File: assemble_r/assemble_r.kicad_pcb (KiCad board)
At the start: 2 copper layers, 57 parts, among them J1 Conn_01x02_Pin, SW29 SW_Push, SW30 SW_Push, SW31 SW_Push, SW32 SW_Push, SW33 SW_Push, SW34 SW_Push, SW35 SW_Push, SW36 SW_Push, SW37 SW_Push, SW38 SW_Push, SW39 SW_Push, SW40 SW_Push, SW41 SW_Push, SW42 SW_Push, SW43 SW_Push, SW44 SW_Push, SW45 SW_Push, SW46 SW_Push, SW47 SW_Push, SW48 SW_Push, SW49 SW_Push, SW50 SW_Push, SW51 SW_Push, SW52 SW_Push, SW53 SW_Push, SW54 SW_Push, SW55 SW_Push, SW56 SW_Push, U1 Micon_BLEMicroPro

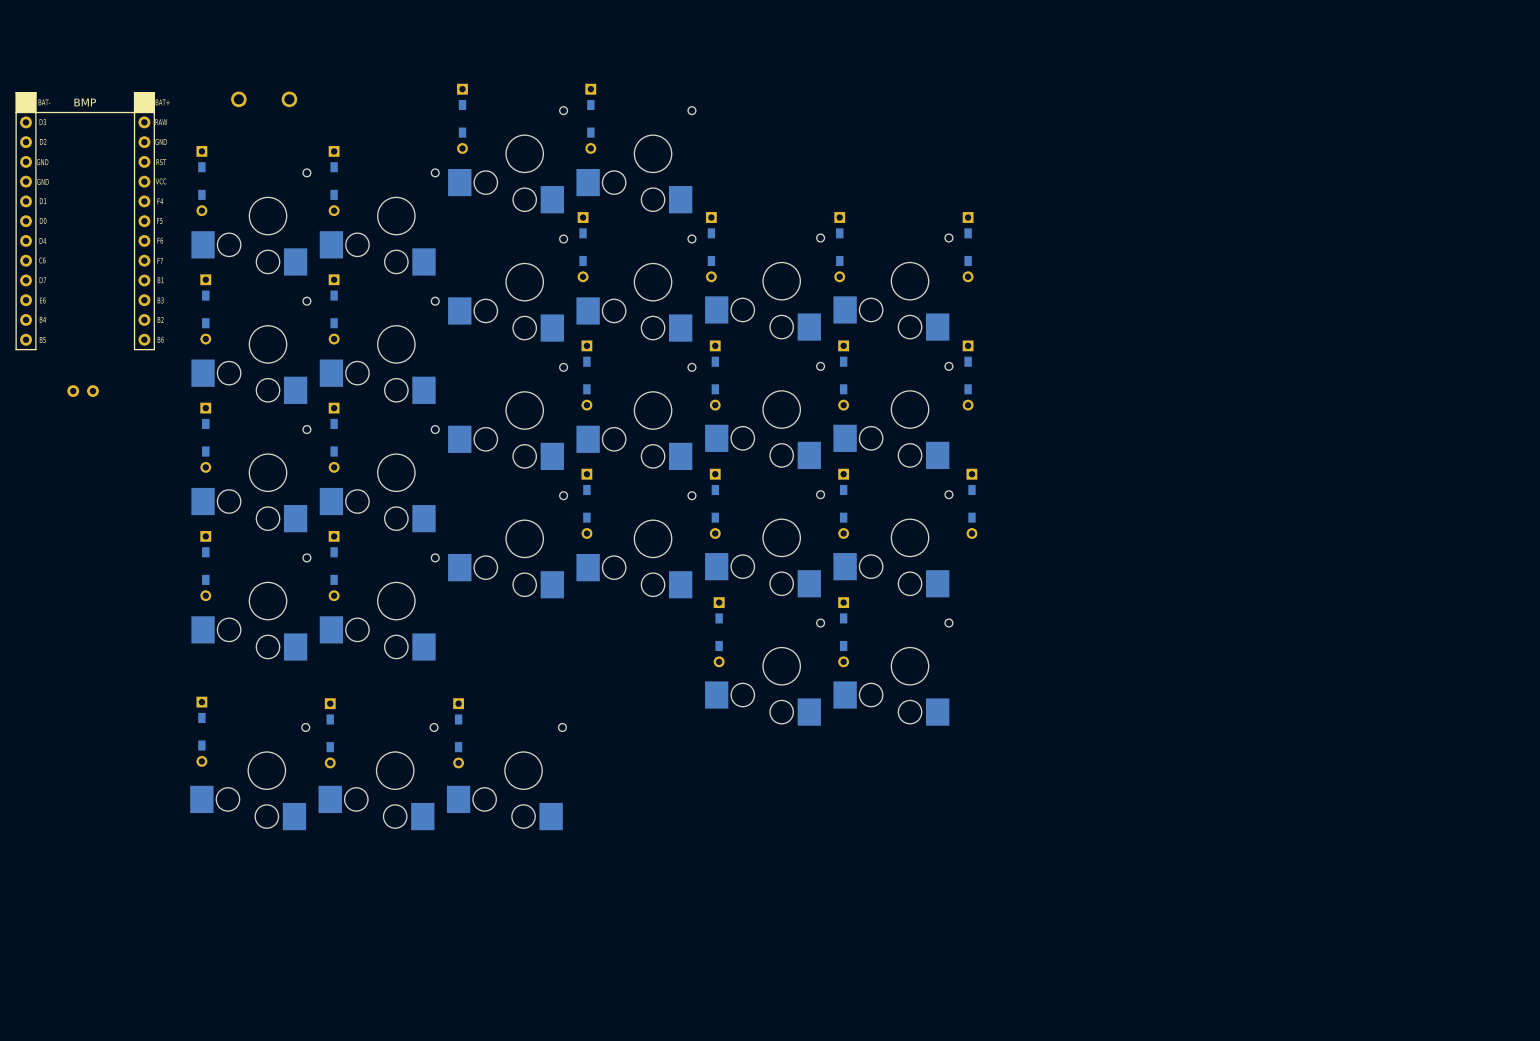
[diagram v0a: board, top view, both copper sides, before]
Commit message: feat: add PCB for right hand
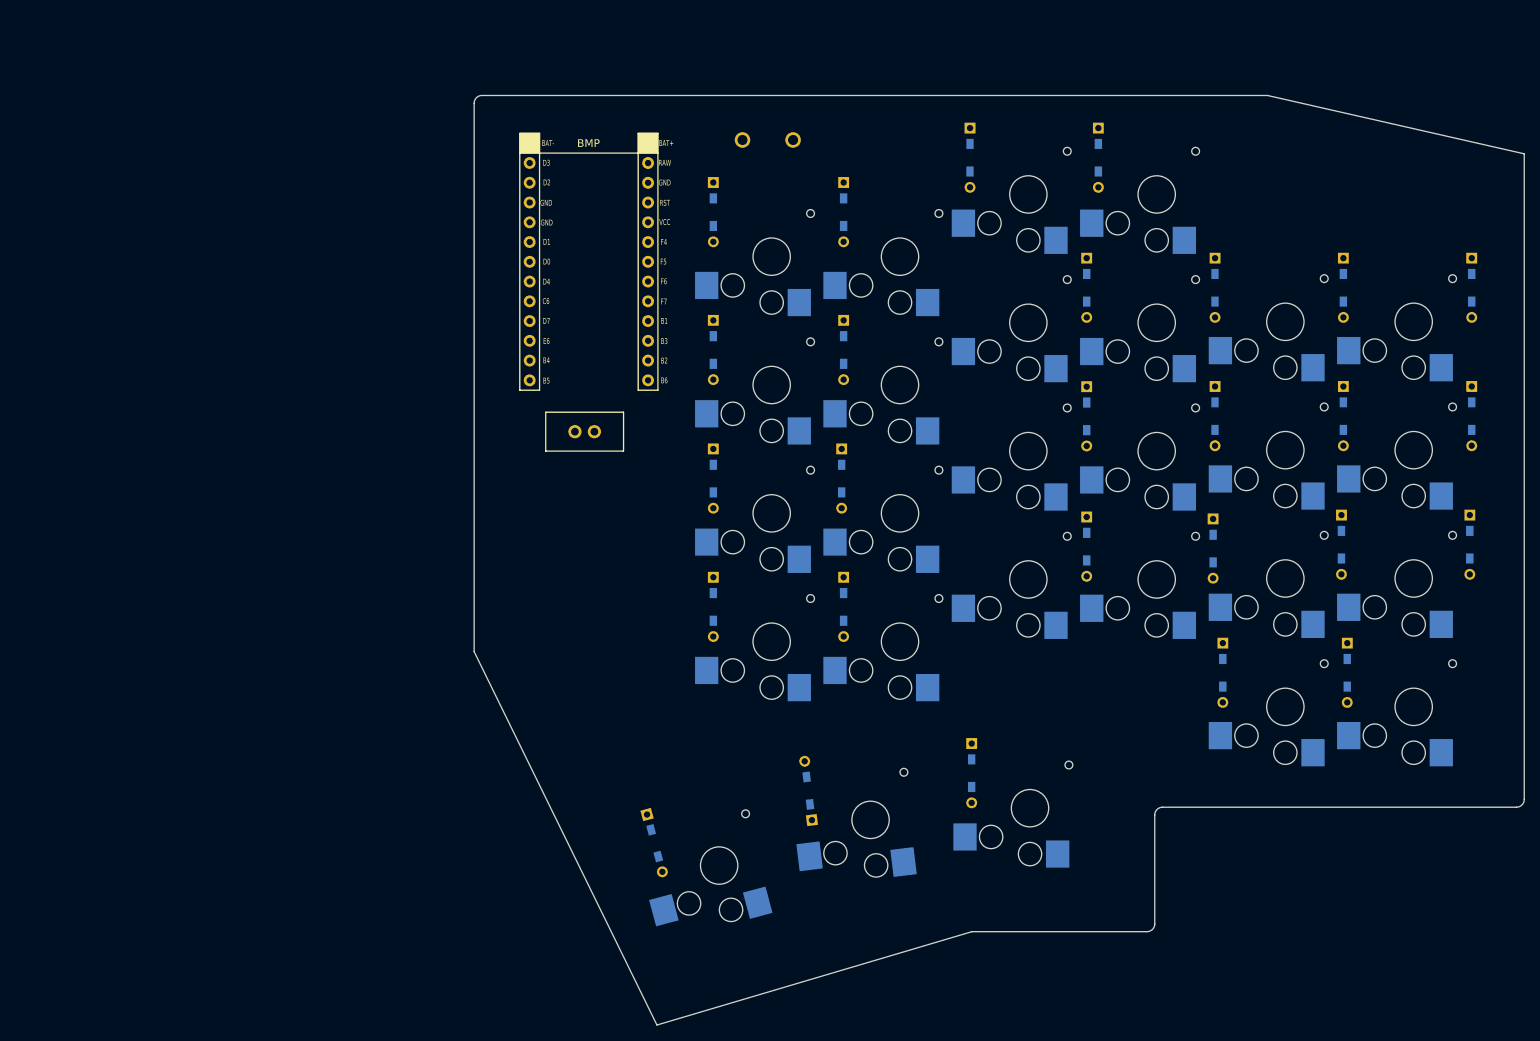
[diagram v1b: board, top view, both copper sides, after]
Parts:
- J1: footprint kbd_Parts:Battery_BMP_2pin -> kbd_Parts:Battery_2pin
- moved D43 66.2 mm to (145.0, 127.1)
- moved D29 65.9 mm to (111.8, 55.0)
- moved D37 65.7 mm to (128.5, 105.8)
- moved D35 65.7 mm to (128.5, 72.7)
- moved D34 65.6 mm to (128.5, 55.0)
- moved D31 65.5 mm to (111.8, 89.2)
- moved D32 65.5 mm to (111.8, 105.8)
- moved D36 65.5 mm to (128.2, 89.2)
- moved D30 65.5 mm to (111.8, 72.7)
- moved D39 65.4 mm to (144.8, 48.0)
- moved D44 65.4 mm to (161.2, 48.0)
- moved SW43 65.3 mm to (152.5, 131.6)
- moved D40 65.0 mm to (159.8, 64.7)
- moved D45 65.0 mm to (176.2, 64.7)
- moved D48 65.0 mm to (192.8, 64.7)
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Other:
- board outline added: 135 x 119.5 mm

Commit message: feat: implement left side
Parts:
- moved SW56 1.30 mm to (118.5, 47.0)
- moved D33 1.00 mm to (104.2, 135.1)
- moved SW33 1.00 mm to (112.5, 138.0)
- moved D43 0.88 mm to (145.0, 128.0), turned to 85 degrees
- moved SW43 0.88 mm to (152.5, 132.5), turned to -5 degrees
- moved J1 0.28 mm to (95.2, 83.5)
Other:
- board size 135 x 119.5 mm -> 135 x 119.3 mm

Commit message: feat: add switch plate
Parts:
- moved SW56 66.0 mm to (87.0, 105.0), turned to 90 degrees
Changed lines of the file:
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@@
 	(footprint "kbd_Parts:ResetSW"
 		(layer "F.Cu")
-		(at 118.5 47)
+		(at 87 105 90)
 		(property "Reference" "SW56"
-			(at 0 2.55 0)
+			(at 0 2.55 90)
 			(layer "F.SilkS")
 			(hide yes)
@@
 		)
 		(property "Value" "SW_Push"
-			(at 0 -2.55 0)
+			(at 0 -2.55 90)
 			(layer "F.Fab")
 			(effects
@@
 		)
 		(property "Datasheet" ""
-			(at 0 0 0)
+			(at 0 0 90)
 			(layer "F.Fab")
 			(hide yes)
@@
 		)
 		(property "Description" "Push button switch, generic, two pins"
-			(at 0 0 0)
+			(at 0 0 90)
 			(layer "F.Fab")
 			(hide yes)
@@
 		(attr through_hole)
 		(fp_line
-			(start -3 -1.75)
-			(end 3 -1.75)
+			(start 3 -1.75)
+			(end 3 -1.5)
 			(stroke
 				(width 0.15)
@@
 		)
 		(fp_line
-			(start -3 -1.5)
-			(end -3 -1.75)
+			(start -3 -1.75)
+			(end 3 -1.75)
 			(stroke
 				(width 0.15)
@@
 		)
 		(fp_line
-			(start -3 1.75)
-			(end -3 1.5)
+			(start -3 -1.5)
+			(end -3 -1.75)
 			(stroke
 				(width 0.15)
@@
 		)
 		(fp_line
-			(start 3 -1.75)
-			(end 3 -1.5)
+			(start 3 1.5)
+			(end 3 1.75)
 			(stroke
 				(width 0.15)
@@
 		)
 		(fp_line
-			(start 3 1.5)
-			(end 3 1.75)
+			(start 3 1.75)
+			(end -3 1.75)
 			(stroke
 				(width 0.15)
@@
 		)
 		(fp_line
-			(start 3 1.75)
-			(end -3 1.75)
+			(start -3 1.75)
+			(end -3 1.5)
 			(stroke
 				(width 0.15)
@@
 		)
 		(fp_text user "RESET"
-			(at 0.127 0 0)
+			(at 0.127 0 90)
 			(layer "B.SilkS")
 			(effects
@@
 		)
 		(pad "1" thru_hole circle
-			(at 3.25 0)
+			(at 3.25 0 90)
 			(size 2 2)
 			(drill 1.3)
@@
 		)
 		(pad "2" thru_hole circle
-			(at -3.25 0)
+			(at -3.25 0 90)
 			(size 2 2)
 			(drill 1.3)
@@
 		)
 		(fp_line
-			(start -3.399998 6.199999)
+			(start -3.399997 6.199999)
 			(end -3.4 1.38)
 			(stroke
@@
 		(fp_line
 			(start 0.35 8.2)
-			(end 0.350001 3.600002)
+			(end 0.350001 3.600003)
 			(stroke
 				(width 0.15)
@@
 		(fp_line
 			(start 1.1 8.2)
-			(end 1.099999 3.6)
+			(end 1.099998 3.6)
 			(stroke
 				(width 0.15)
@@
 		)
 		(fp_line
-			(start 1.3 3.575002)
+			(start 1.3 3.575003)
 			(end -1.275 3.575)
 			(stroke
@@
 		(fp_line
 			(start 2.299999 4.574999)
-			(end 1.3 3.575002)
+			(end 1.3 3.575003)
 			(stroke
 				(width 0.15)

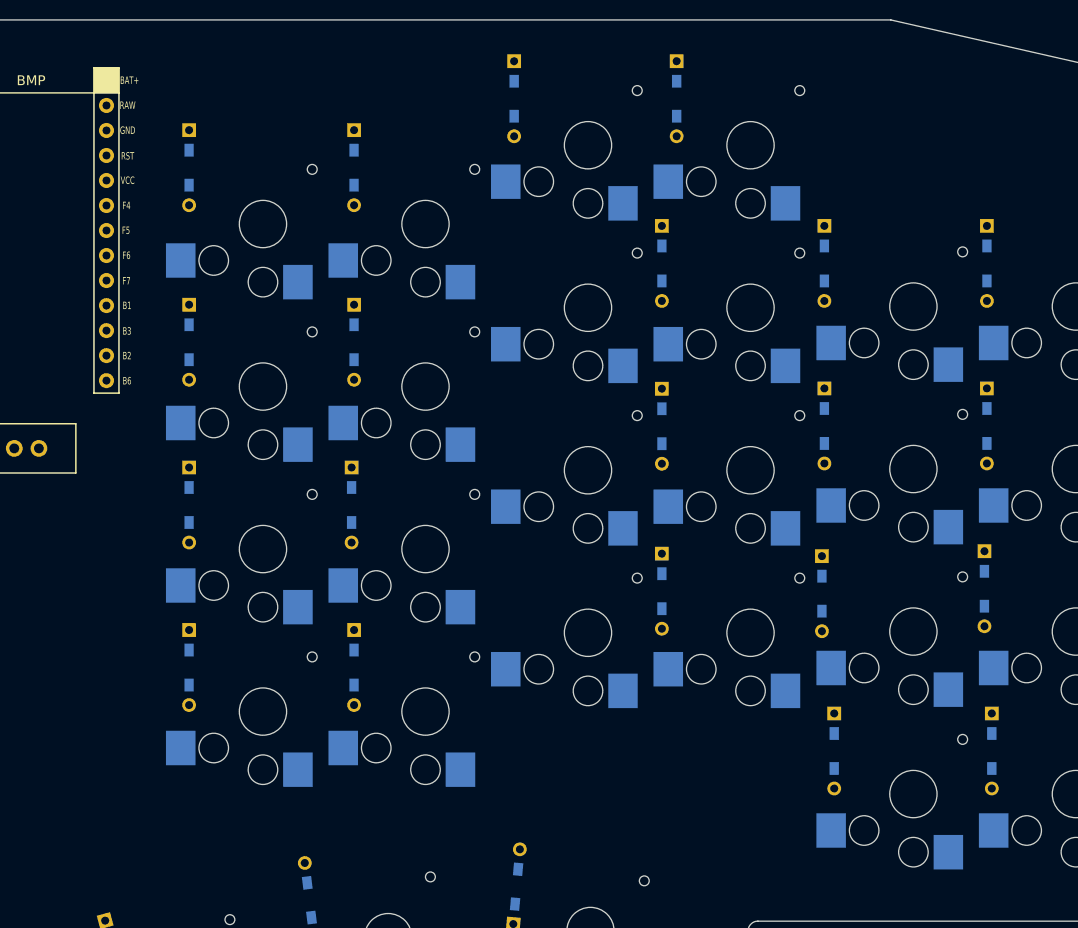
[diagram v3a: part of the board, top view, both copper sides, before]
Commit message: feat: add hole to switch plate
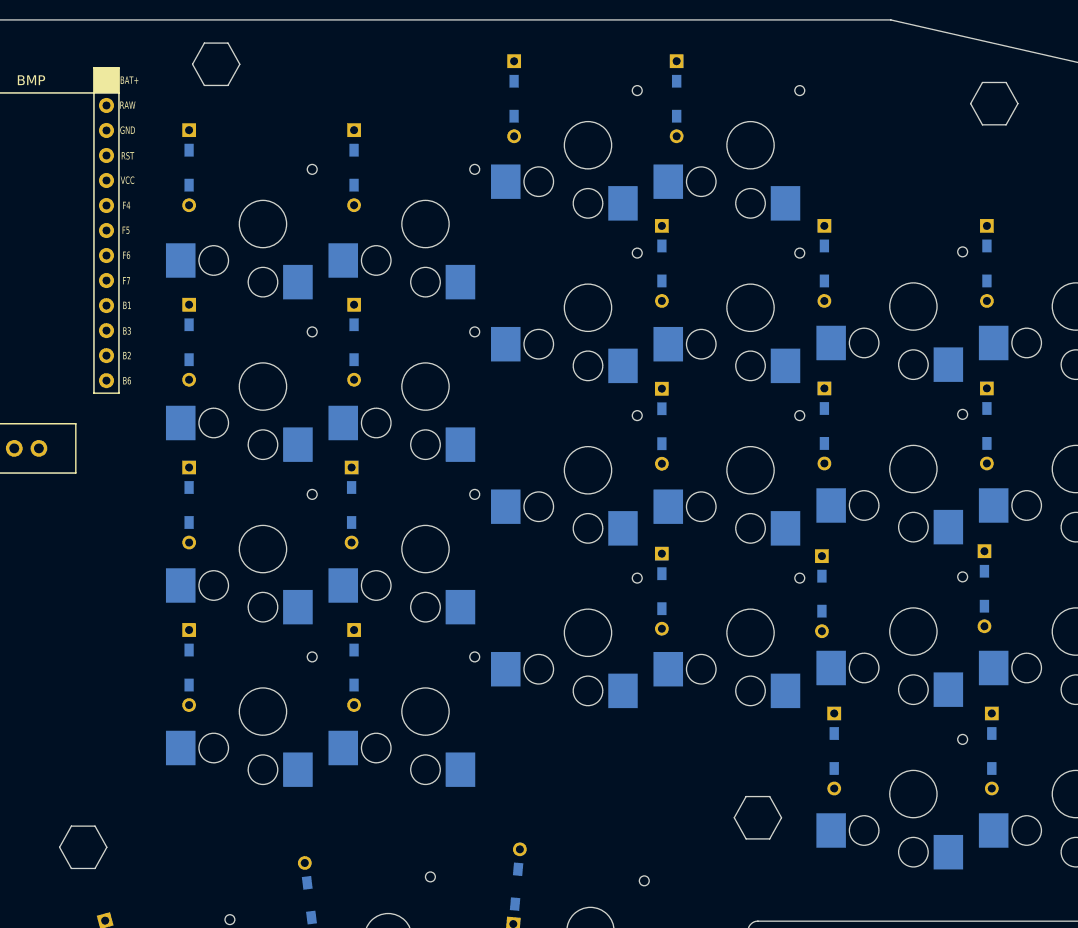
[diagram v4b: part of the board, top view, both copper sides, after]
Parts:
- added Ref**: Val**, kbd_Hole:m2_Spacer_Hole_hex, F.Cu at (193.5, 48.5)
- added Ref**: Val**, kbd_Hole:m2_Spacer_Hole_hex, F.Cu at (114.5, 44.5)
- added Ref**: Val**, kbd_Hole:m2_Spacer_Hole_hex, F.Cu at (169.5, 121.0)
- added Ref**: Val**, kbd_Hole:m2_Spacer_Hole_hex, F.Cu at (101.0, 124.0)
